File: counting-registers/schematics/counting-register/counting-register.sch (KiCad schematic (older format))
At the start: 27 parts

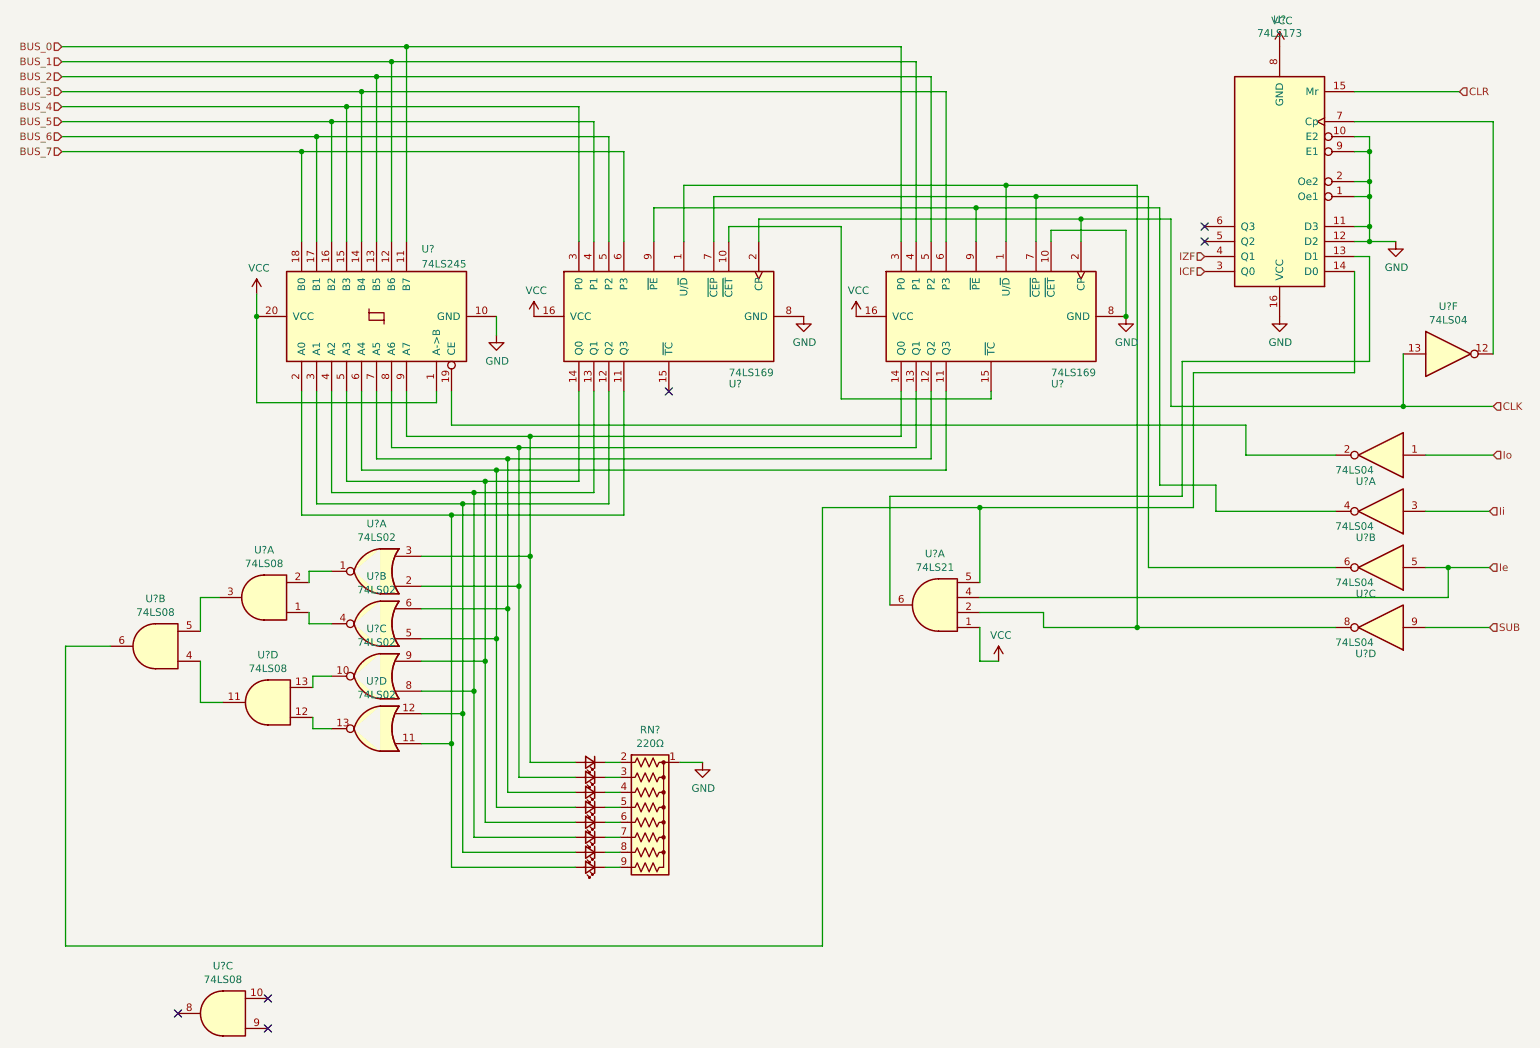
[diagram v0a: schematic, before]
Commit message: improvements to counting register documentation
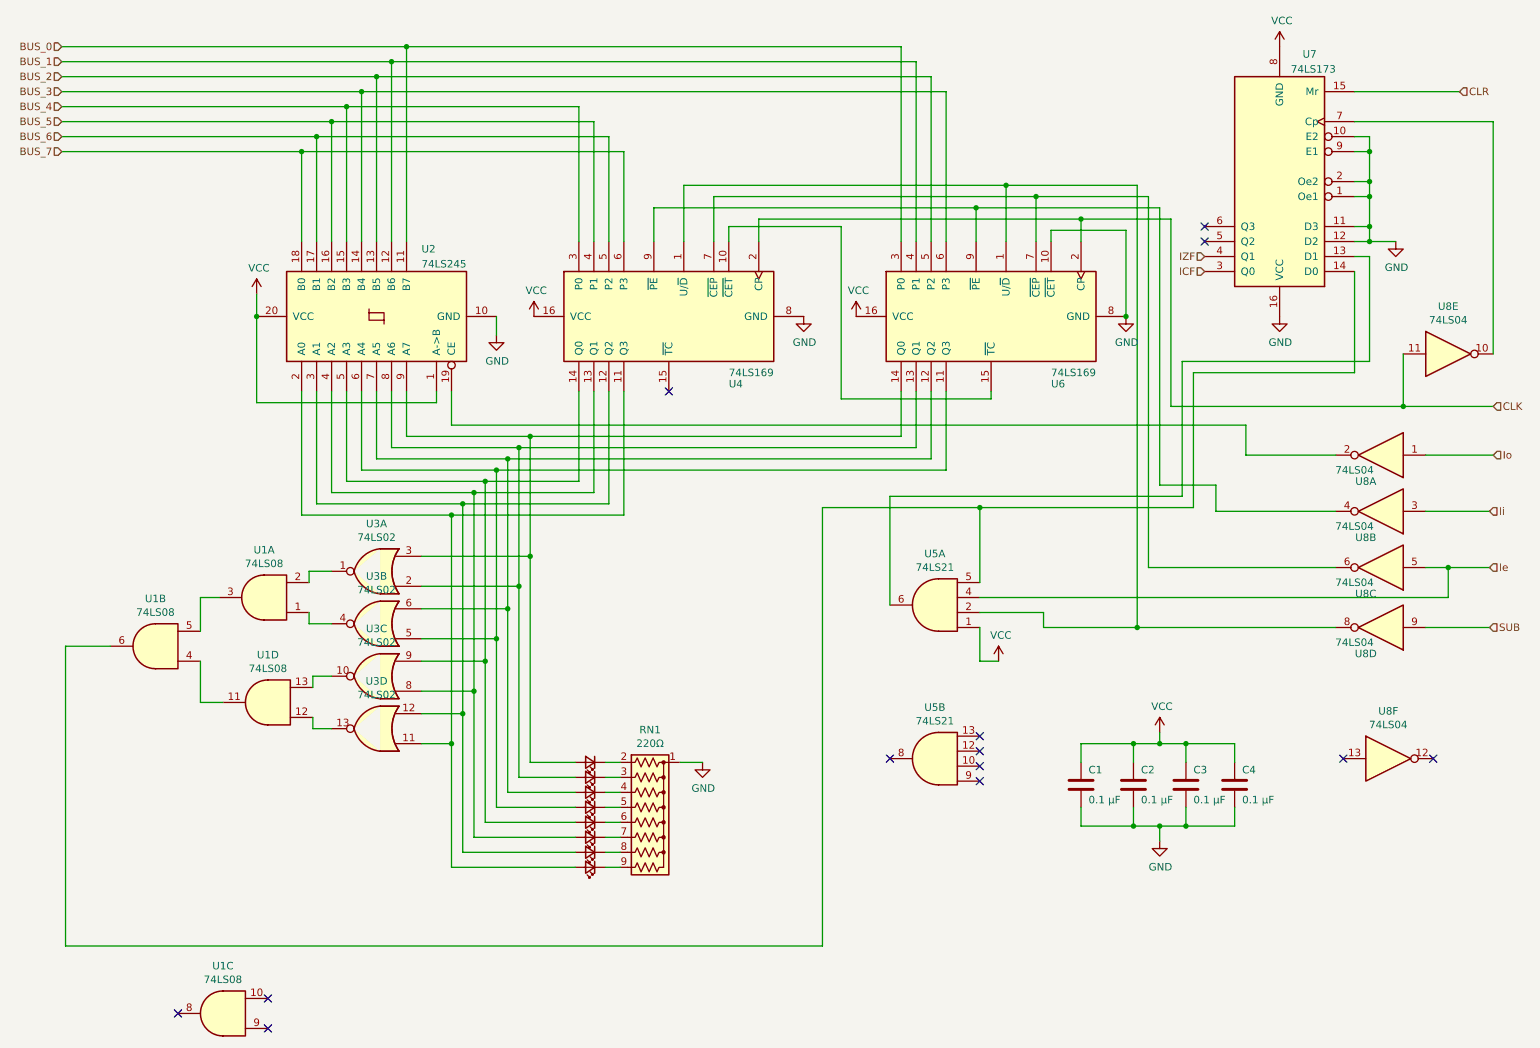
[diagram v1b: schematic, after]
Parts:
- added C1, C2, C3, C4: 0.1 µF, symbol Device:C
- added unit 2 of U5
- added unit 5 of U8
- gave numbers to parts that had none: 17
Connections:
- net CLK: now also U8.11; no longer U8.13
- net GND: now also C1.2, C2.2, C3.2, C4.2
- net VCC: now also C1.1, C2.1, C3.1, C4.1
- net at U7.7 (Cp): now also U8.10; no longer U8.12
- no-connect marks 6 -> 13
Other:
- moved on the sheet: U8F
